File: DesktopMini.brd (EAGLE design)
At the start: 44.1 x 32.5 mm, 38 parts, among them J1 CONN_82.54_SCREW, J2 CONN_3, U1 ADS1115, U2 ATMEGA328P_TQFP, U3 SN74LVC1G17DCK, U4 FT232RL, U5 MIC2091, U6 MIC53653.3SC70, Y1 16MHz

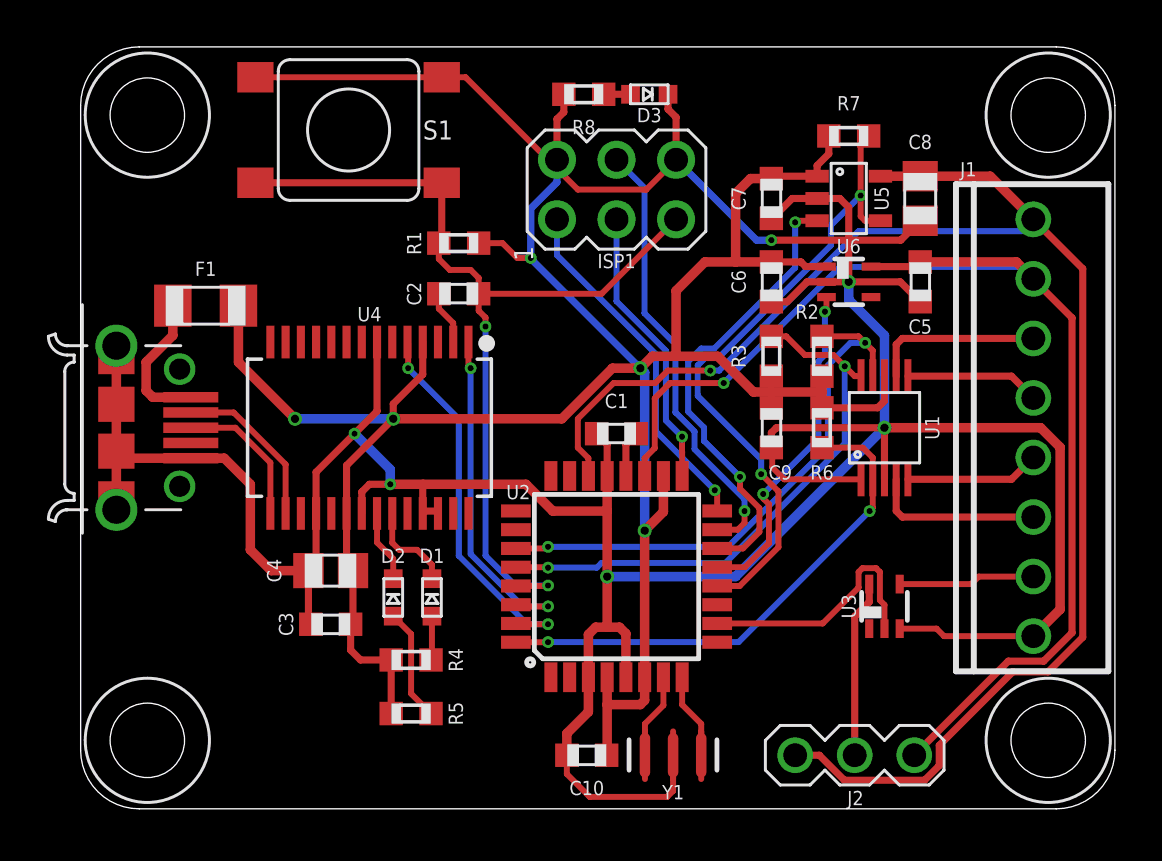
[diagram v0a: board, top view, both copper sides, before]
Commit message: Minor updates, v0.0 to fab
Added auxiliary LED and did minor cleanup, added BMP image via script
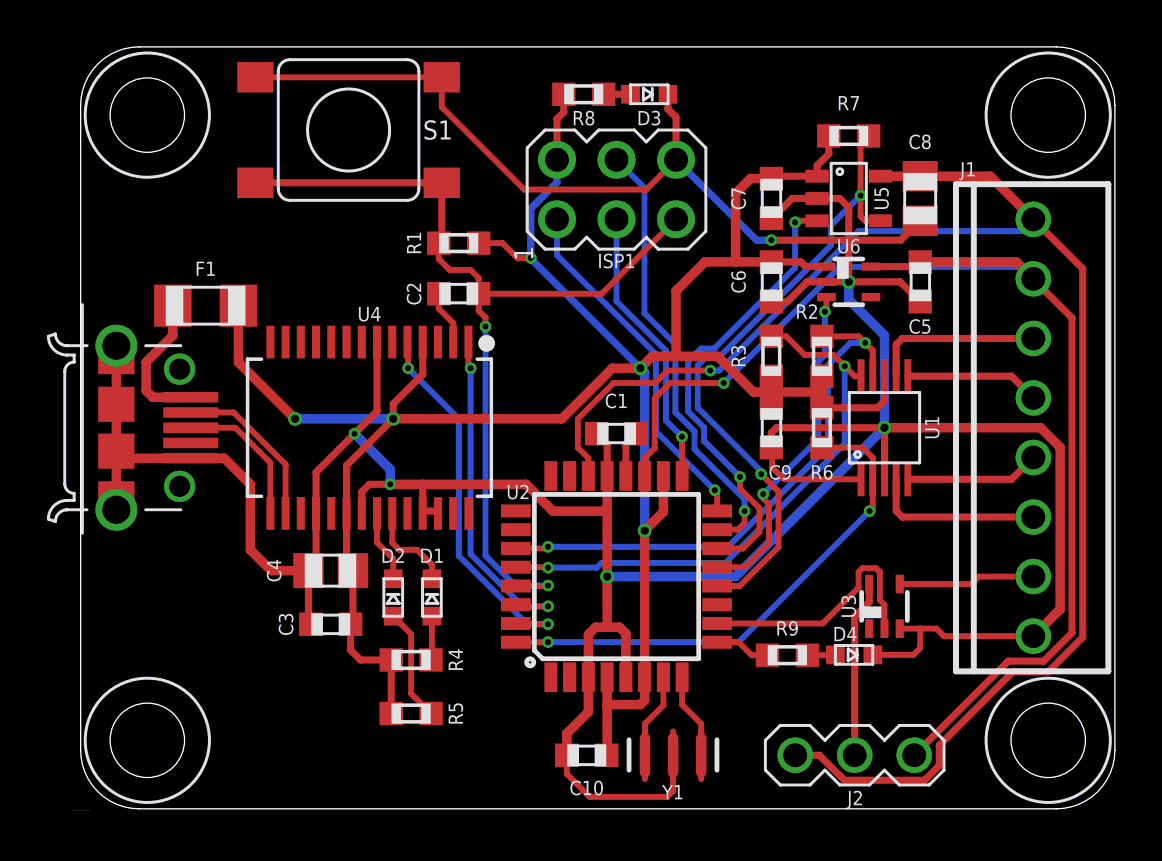
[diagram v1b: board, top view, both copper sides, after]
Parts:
- added D4: LEDBLUE0603, bschulz:LED_0603
- added R9: 330, bschulz_passives:R0603
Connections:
- new net AUX_LED: R9.2, U2.9
- new net N$11: D4.ANODE, R9.1
- net GND: now also D4.CATHODE
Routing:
- net GND: track 178.9 -> 182.7 mm
- net AUX_LED: track 0.00 -> 2.38 mm
- net N$11: track 0.00 -> 1.20 mm
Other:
- board text added: "/Volumes/OSX_Storage/Downloads/Untitled.bmp"
- board text added: "AUX"
